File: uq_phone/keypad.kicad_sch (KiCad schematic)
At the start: 20 parts, among them SW1 SKTAAAE010, SW2 SKTAAAE010

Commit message: Routing Init
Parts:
- renumbered LED16 to LED1, LED5 to LED10, LED2 to LED11, LED17 to LED12, LED15 to LED13, LED12 to LED14, LED9 to LED15, LED6 to LED16, LED3 to LED17, LED13 to LED2, LED10 to LED3, LED7 to LED4, LED4 to LED5, LED1 to LED6, LED14 to LED7, LED11 to LED8, LED8 to LED9, R33 to R48

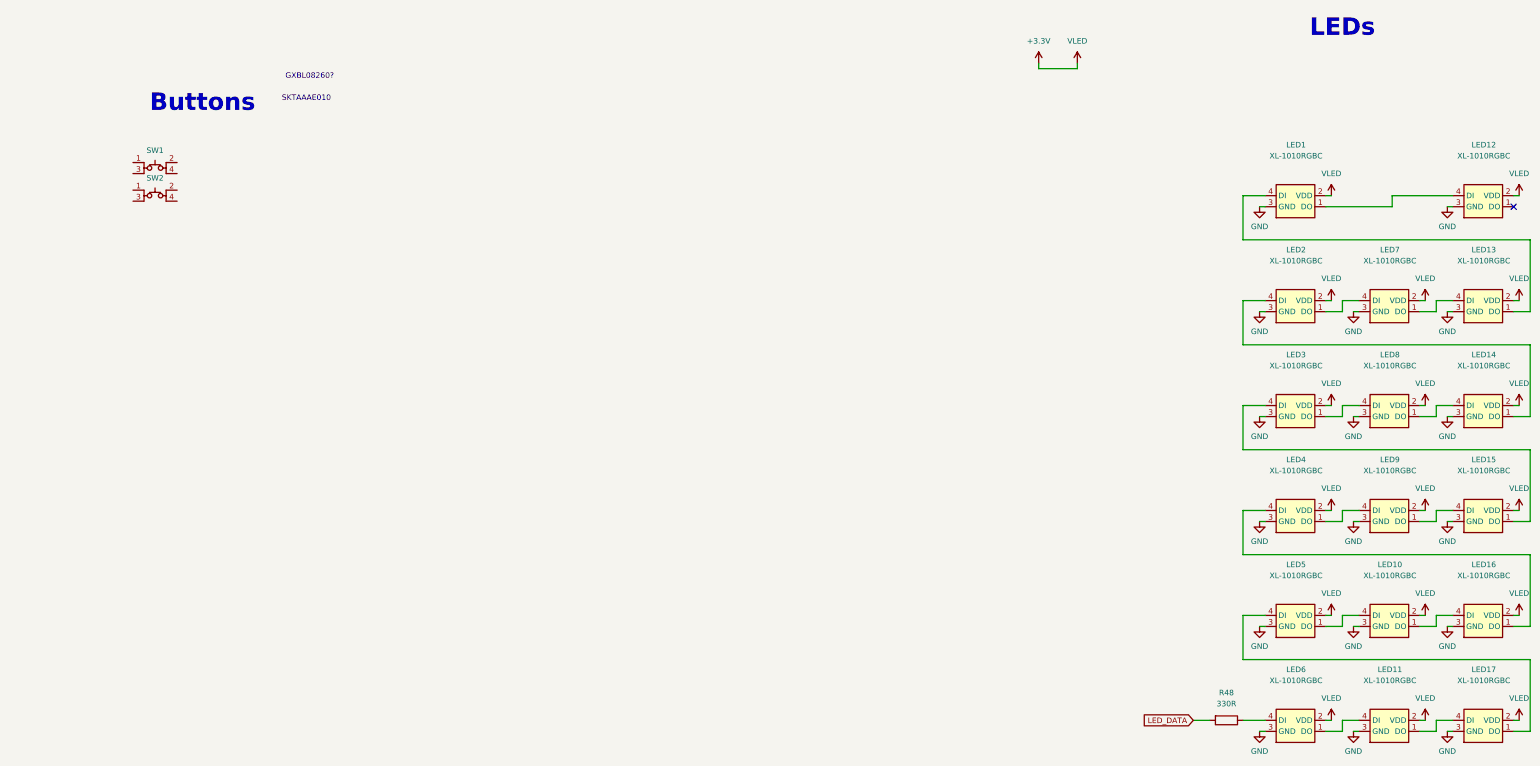
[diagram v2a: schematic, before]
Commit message: Update pcb and remove Stm32 profile
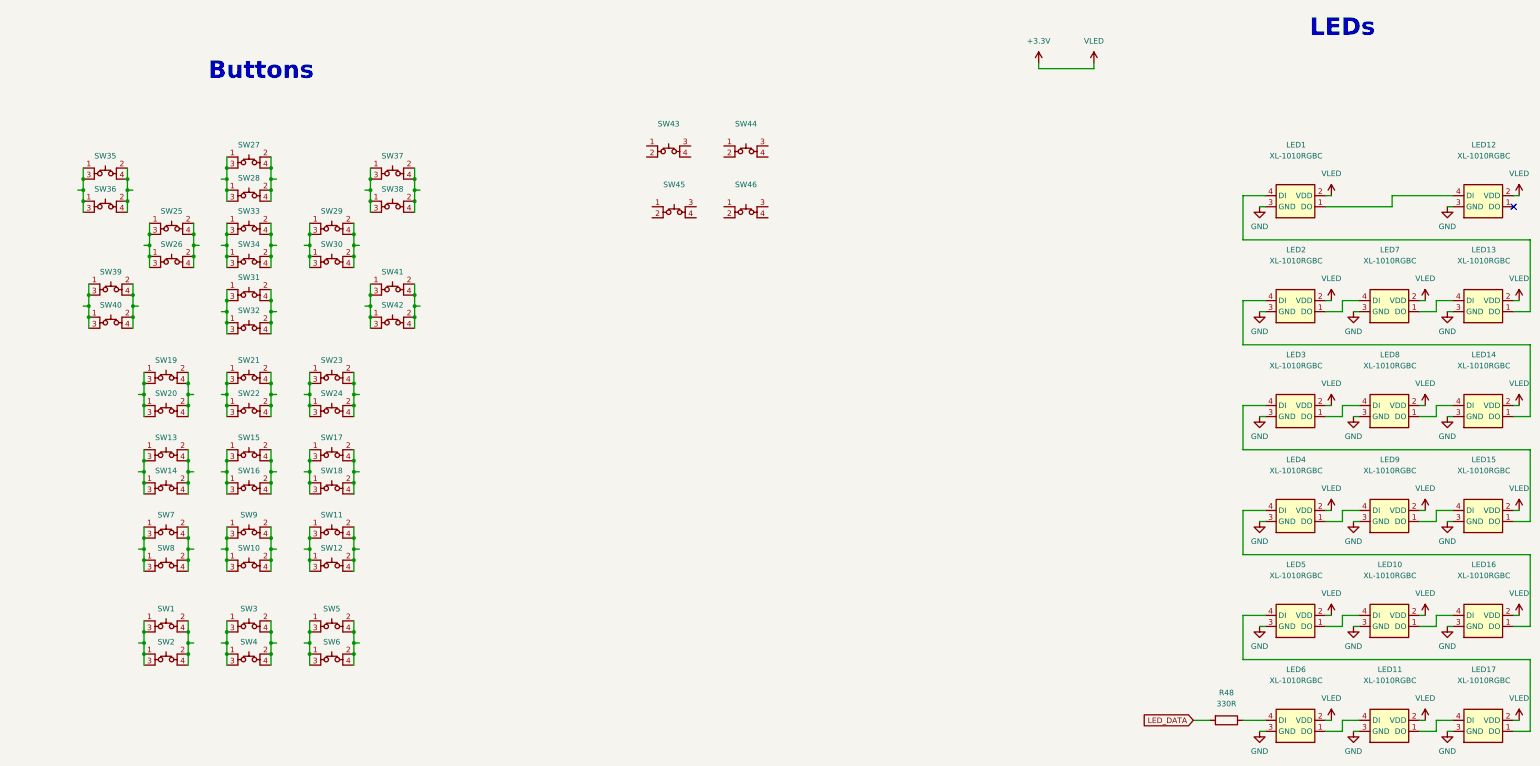
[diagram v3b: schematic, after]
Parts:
- added SW10, SW11, SW12, SW13, SW14, SW15, SW16, SW17, SW18, SW19, SW20, SW21, SW22, SW23, SW24, SW25, SW26, SW27, SW28, SW29, SW3, SW30, SW31, SW32, SW33, SW34, SW35, SW36, SW37, SW38, SW39, SW4, SW40, SW41, SW42, SW5, SW6, SW7, SW8, SW9: SKTAAAE010, custom_footprints:SKTAAAE010, symbol Misc:SKTAAAE010
- added SW43, SW44, SW45, SW46: SKSCLCE010, custom_footprints:SKSCLCE010, symbol Misc:SKSCLCE010
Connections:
- net at SW2.1: now also SW1.1, SW1.3, SW2.3
- net at SW2.2: now also SW1.2, SW1.4, SW2.4
- new net: SW37.1, SW37.3, SW38.1, SW38.3
- new net: SW37.2, SW37.4, SW38.2, SW38.4
- new net: SW35.1, SW35.3, SW36.1, SW36.3
- new net: SW35.2, SW35.4, SW36.2, SW36.4
- new net: SW39.1, SW39.3, SW40.1, SW40.3
- new net: SW39.2, SW39.4, SW40.2, SW40.4
- new net: SW10.1, SW10.3, SW9.1, SW9.3
- new net: SW10.2, SW10.4, SW9.2, SW9.4
- new net: SW31.1, SW31.3, SW32.1, SW32.3
- new net: SW31.2, SW31.4, SW32.2, SW32.4
- new net: SW3.1, SW3.3, SW4.1, SW4.3
- new net: SW3.2, SW3.4, SW4.2, SW4.4
- new net: SW21.1, SW21.3, SW22.1, SW22.3
- new net: SW21.2, SW21.4, SW22.2, SW22.4
- new net: SW5.1, SW5.3, SW6.1, SW6.3
- new net: SW5.2, SW5.4, SW6.2, SW6.4
- new net: SW41.1, SW41.3, SW42.1, SW42.3
- new net: SW41.2, SW41.4, SW42.2, SW42.4
- new net: SW29.1, SW29.3, SW30.1, SW30.3
- new net: SW29.2, SW29.4, SW30.2, SW30.4
- new net: SW23.1, SW23.3, SW24.1, SW24.3
- new net: SW23.2, SW23.4, SW24.2, SW24.4
- new net: SW15.1, SW15.3, SW16.1, SW16.3
- new net: SW15.2, SW15.4, SW16.2, SW16.4
- new net: SW7.1, SW7.3, SW8.1, SW8.3
- new net: SW7.2, SW7.4, SW8.2, SW8.4
- new net: SW33.1, SW33.3, SW34.1, SW34.3
- new net: SW33.2, SW33.4, SW34.2, SW34.4
- new net: SW27.1, SW27.3, SW28.1, SW28.3
- new net: SW27.2, SW27.4, SW28.2, SW28.4
- new net: SW17.1, SW17.3, SW18.1, SW18.3
- new net: SW17.2, SW17.4, SW18.2, SW18.4
- new net: SW19.1, SW19.3, SW20.1, SW20.3
- new net: SW19.2, SW19.4, SW20.2, SW20.4
- new net: SW11.1, SW11.3, SW12.1, SW12.3
- new net: SW11.2, SW11.4, SW12.2, SW12.4
- new net: SW25.1, SW25.3, SW26.1, SW26.3
- new net: SW25.2, SW25.4, SW26.2, SW26.4
- new net: SW13.1, SW13.3, SW14.1, SW14.3
- new net: SW13.2, SW13.4, SW14.2, SW14.4
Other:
- note removed: "GXBL08260?"
- note removed: "SKTAAAE010"
- moved on the sheet: SW1, SW2

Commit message: Update Keypad
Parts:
- removed SW26, SW28, SW30, SW32: SKTAAAE010, custom_footprints:SKTAAAE010, symbol Misc:SKTAAAE010
- removed SW46: SKSCLCE010, custom_footprints:SKSCLCE010, symbol Misc:SKSCLCE010
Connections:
- net GND: now also SW1.2, SW1.4, SW10.2, SW10.4, SW11.2, SW11.4, SW12.2, SW12.4, SW13.2, SW13.4, SW14.2, SW14.4, SW15.2, SW15.4, SW16.2, SW16.4, SW17.2, SW17.4, SW18.2, SW18.4, SW19.2, SW19.4, SW2.2, SW2.4, SW20.2, SW20.4, SW21.2, SW21.4, SW22.2, SW22.4, SW23.2, SW23.4, SW24.2, SW24.4, SW25.2, SW25.4, SW27.2, SW27.4, SW29.2, SW29.4, SW3.2, SW3.4, SW31.2, SW31.4, SW33.2, SW33.4, SW34.2, SW34.4, SW35.2, SW35.4, SW36.2, SW36.4, SW37.2, SW37.4, SW38.2, SW38.4, SW39.2, SW39.4, SW4.2, SW4.4, SW40.2, SW40.4, SW41.2, SW41.4, SW42.2, SW42.4, SW43.3, SW43.4, SW44.3, SW44.4, SW45.3, SW45.4, SW5.2, SW5.4, SW6.2, SW6.4, SW7.2, SW7.4, SW8.2, SW8.4, SW9.2, SW9.4
- net PB_MENU_R: now reaches SW37.1, SW37.3, SW38.1, SW38.3
- net PB_MENU_L: now reaches SW35.1, SW35.3, SW36.1, SW36.3
- net PB_CALL: now reaches SW39.1, SW39.3, SW40.1, SW40.3
- net PB_VOL_DOWN: now reaches SW45.1
- net PB_VOL_DOWN: now also SW45.2
- net PB_2: now reaches SW10.1, SW10.3, SW9.1, SW9.3
- net PB_DPAD_DOWN: now reaches SW31.1, SW31.3
- net PB_0: now reaches SW3.1, SW3.3, SW4.1, SW4.3
- net PB_8: now reaches SW21.1, SW21.3, SW22.1, SW22.3
- net PB_HASH: now reaches SW5.1, SW5.3, SW6.1, SW6.3
- net PB_END_CALL: now reaches SW41.1, SW41.3, SW42.1, SW42.3
- net PB_STAR: now reaches SW1.1, SW1.3, SW2.1, SW2.3
- net PB_DPAD_RIGHT: now reaches SW29.1, SW29.3
- net PB_9: now reaches SW23.1, SW23.3, SW24.1, SW24.3
- net PB_5: now reaches SW15.1, SW15.3, SW16.1, SW16.3
- net PB_1: now reaches SW7.1, SW7.3, SW8.1, SW8.3
- net PB_DPAD_SELECT: now reaches SW33.1, SW33.3, SW34.1, SW34.3
- net PB_DPAD_UP: now reaches SW27.1, SW27.3
- net PB_6: now reaches SW17.1, SW17.3, SW18.1, SW18.3
- net PB_7: now reaches SW19.1, SW19.3, SW20.1, SW20.3
- net PB_VOL_UP: now reaches SW43.1
- net PB_VOL_UP: now also SW43.2
- net PB_PWR: now reaches SW44.1
- net PB_PWR: now also SW44.2
- net PB_3: now reaches SW11.1, SW11.3, SW12.1, SW12.3
- net PB_DPAD_LEFT: now reaches SW25.1, SW25.3
- net PB_4: now reaches SW13.1, SW13.3, SW14.1, SW14.3
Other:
- note added: "D-Pad Buttons"
- note added: "Keypad Buttons"
- note added: "Menu/Call Buttons"
- note added: "Side Buttons"
- moved on the sheet: SW1, SW10, SW11, SW12, SW13, SW14, SW15, SW16, SW17, SW18, SW19, SW2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

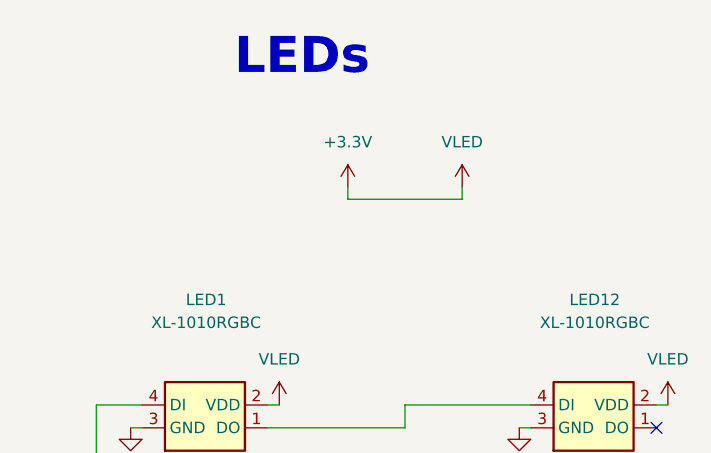
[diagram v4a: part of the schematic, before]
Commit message: Add Front Pannel Suboard and connector
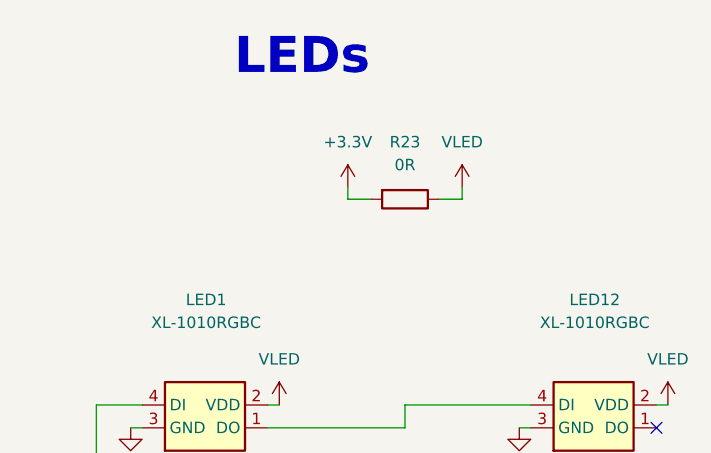
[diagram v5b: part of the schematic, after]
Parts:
- added R23: 0R, Resistor_SMD:R_0603_1608Metric, symbol Resistors:Resistor_0R
- LED1, LED10, LED11, LED12, LED13, LED14, LED15, LED16, LED17, LED2, LED3, LED4, LED5, LED6, LED7, LED8, LED9, R48, SW1, SW10, SW11, SW12, SW13, SW14, SW15, SW16, SW17, SW18, SW19, SW2, SW20, SW21, SW22, SW23, SW24, SW25, SW27, SW29, SW3, SW31, SW33, SW34, SW35, SW36, SW37, SW38, SW39, SW4, SW40, SW41, SW42, SW43, SW44, SW45, SW5, SW6, SW7, SW8, SW9: now left out of the parts list
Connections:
- net +3.3V: now also R23.2; no longer LED1.2 (VDD), LED10.2 (VDD), LED11.2 (VDD), LED12.2 (VDD), LED13.2 (VDD), LED14.2 (VDD), LED15.2 (VDD), LED16.2 (VDD), LED17.2 (VDD), LED2.2 (VDD), LED3.2 (VDD), LED4.2 (VDD), LED5.2 (VDD), LED6.2 (VDD), LED7.2 (VDD), LED8.2 (VDD), LED9.2 (VDD)
- new net VLED: LED1.2 (VDD), LED10.2 (VDD), LED11.2 (VDD), LED12.2 (VDD), LED13.2 (VDD), LED14.2 (VDD), LED15.2 (VDD), LED16.2 (VDD), LED17.2 (VDD), LED2.2 (VDD), LED3.2 (VDD), LED4.2 (VDD), LED5.2 (VDD), LED6.2 (VDD), LED7.2 (VDD), LED8.2 (VDD), LED9.2 (VDD), R23.1

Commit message: Clean up and add DNP
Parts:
- LED1, LED10, LED11, LED12, LED13, LED14, LED15, LED16, LED17, LED2, LED3, LED4, LED5, LED6, LED7, LED8, LED9, R23, R48, SW1, SW10, SW11, SW12, SW13, SW14, SW15, SW16, SW17, SW18, SW19, SW2, SW20, SW21, SW22, SW23, SW24, SW25, SW27, SW29, SW3, SW31, SW33, SW34, SW35, SW36, SW37, SW38, SW39, SW4, SW40, SW41, SW42, SW43, SW44, SW45, SW5, SW6, SW7, SW8, SW9: now not fitted

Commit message: Generate Early production outputs
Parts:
- R23: LCSC PN (none) -> C95177
- R48: LCSC PN (none) -> C6117577
